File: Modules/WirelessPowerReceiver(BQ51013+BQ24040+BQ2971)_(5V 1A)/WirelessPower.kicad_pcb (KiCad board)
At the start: 4 copper layers, 56 x 56 mm, 46 parts, among them J1 Conn_01x01_Female, J2 Conn_01x01_Female, J3 Conn_01x01_Female, J4 Conn_01x01_Female, J6 AC, J7 Conn_01x14, U1 BQ2971, U2 BQ51013BRHLR, U3 CSD16406Q3, U4 CSD16406Q3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

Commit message: update WirelessPower PCB LAYOUT
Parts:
- moved C15 1.26 mm to (164.9, 114.4)
- moved C2 1.19 mm to (164.9, 115.6)
- moved C19 0.99 mm to (164.1, 112.4)
- moved J6 0.91 mm to (171.4, 111.1)
- moved C14 0.88 mm to (163.0, 112.4)
- moved C13 0.77 mm to (161.8, 112.4)
- moved C1 0.46 mm to (160.1, 112.4)
- moved C22 0.24 mm to (168.5, 113.9)
- moved C20 0.22 mm to (158.4, 112.4)
- moved C10 0.12 mm to (168.5, 115.0)
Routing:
- net Net-(C1-Pad1): track 1552.8 -> 1899.7 mm
- net Net-(C15-Pad2): track 117.3 -> 41.2 mm
- net Net-(C1-Pad2): track 88.2 -> 71.3 mm
- net REG_power: track 53.0 -> 54.7 mm
- net BAT_PG: track 22.2 -> 23.2 mm
- net BAT_ISET: track 29.3 -> 30.2 mm
- net BAT_CHG: track 32.1 -> 32.6 mm

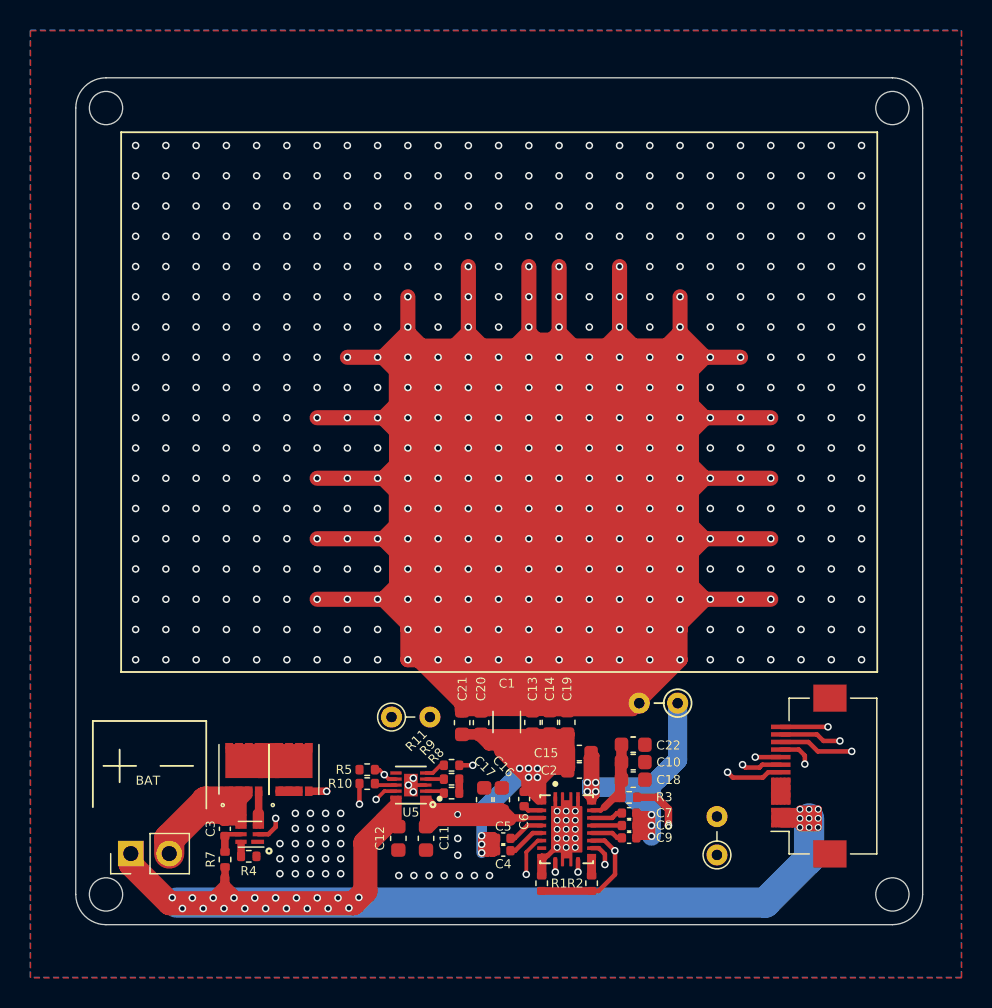
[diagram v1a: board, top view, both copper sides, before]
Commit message: update WirelessPower.sch by kicad6
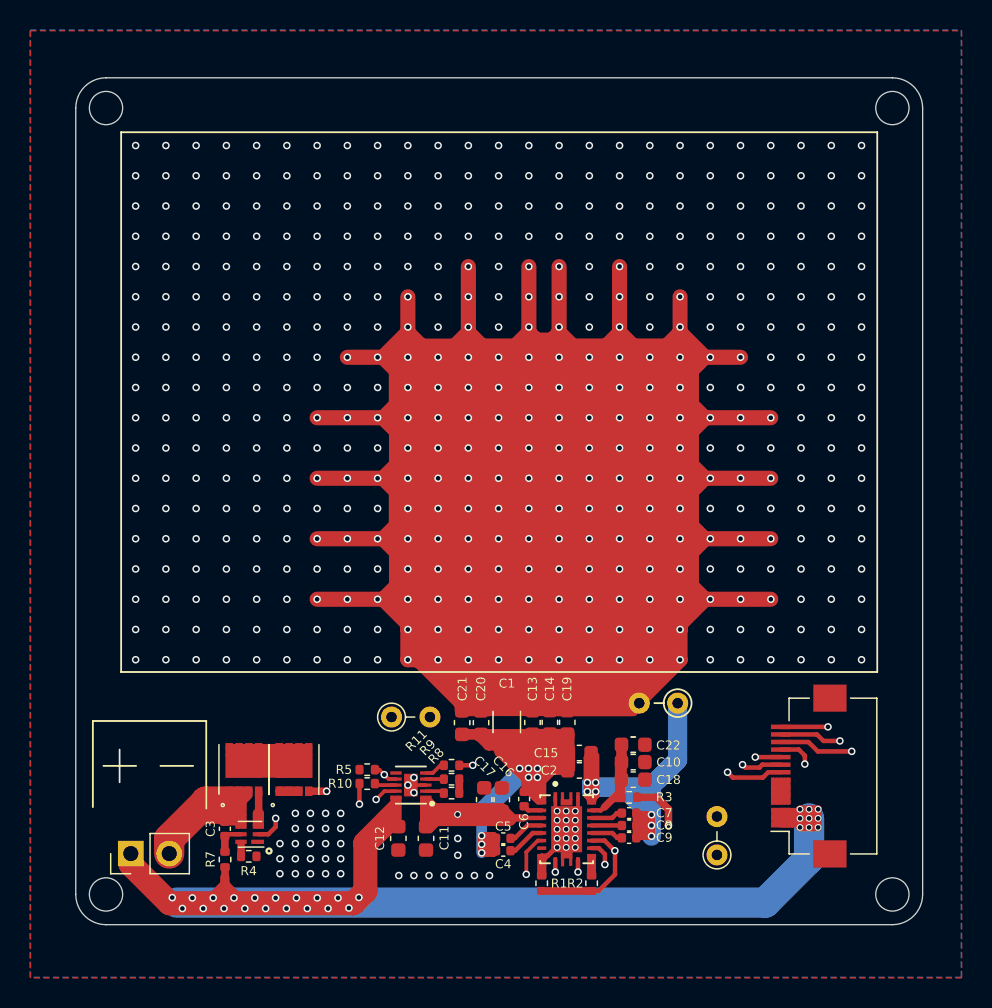
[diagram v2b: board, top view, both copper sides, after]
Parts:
- R2: value 15R -> 20R
- R8: value 640R -> 536R
- renumbered BAT to J5
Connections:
- U1 pad 1: (no net) -> unconnected-(U1-Pad1)
- U2 pad 8: (no net) -> unconnected-(U2-Pad8)
- U5 pad 6: (no net) -> unconnected-(U5-Pad6)
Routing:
- net Net-(U3-Pad5): track 11.4 -> 16.3 mm
- net Net-(C1-Pad1): track 1899.7 -> 1903.7 mm
- net REG_power: track 54.7 -> 52.7 mm
- net BAT+: track 161.4 -> 160.2 mm
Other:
- net class Default removed

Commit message: update WirelessPower layout
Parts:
- moved C16 0.36 mm to (160.1, 117.5)
- moved C19 0.30 mm to (164.4, 112.4)
- moved C17 0.29 mm to (158.9, 117.5)
- moved C2 0.27 mm to (164.9, 115.9)
- moved C22 0.22 mm to (168.5, 113.7)
- moved C1 0.15 mm to (160.1, 112.2)
- moved C14 0.15 mm to (163.1, 112.4)
- moved C15 0.13 mm to (164.9, 114.6)
- moved R11 0.11 mm to (156.3, 115.2)
- moved R8 0.11 mm to (156.3, 117.1)
- moved R9 0.11 mm to (156.3, 116.2)
- moved C10 0.10 mm to (168.5, 114.9)
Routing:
- net BAT+: track 160.2 -> 114.2 mm
- net Net-(C1-Pad2): track 70.8 -> 80.3 mm, vias 8 -> 9
- net Net-(C10-Pad2): track 10.8 -> 7.77 mm
- net Net-(C15-Pad2): track 40.9 -> 38.8 mm
- net Net-(U1-Pad2): track 7.82 -> 6.49 mm
- net GND: vias 346 -> 344
